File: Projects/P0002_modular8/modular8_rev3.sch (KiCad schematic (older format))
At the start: 14 parts

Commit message: started P0003 LED display, P0002 PCB layout
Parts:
- removed Y?: 16MHz, symbol Crystal_Small
- added C3: 0.1uF, Capacitors_SMD:C_0805, symbol C
- added D1: POW, LEDs:LED-0805, symbol LED
- added D2: SCK, LEDs:LED-0805, symbol LED
- added R1, R2: 680, Resistors_SMD:R_0805, symbol R
- added R3: 10k, Resistors_SMD:R_0805, symbol R
- added R4, R5: 39, Resistors_SMD:R_0805, symbol R
- added U1: LM4040D20IDBZR, Housings_SOT-23_SOT-143_TSOT-6:SOT-23, symbol LM4040D20IDBZR
- added XTAL?1: ABM8-16.000MHZ-10-1-U-T, Libraries - KiCAD:CSMD-ABM8, symbol ABM8-16.000MHZ-10-1-U-T
- C1, C2, C4, C5, C6: renamed from C?; footprint (none) -> Capacitors_SMD:C_0805
- GC1: renamed from GC; footprint (none) -> Resistors_SMD:R_0805
- IC1: renamed from IC?; footprint MLF/QFN32 -> Housings_QFP:TQFP-32_7x7mm_Pitch0.8mm
- J1, J2, J3, J4: renamed from J?; footprint (none) -> Libraries - KiCAD:modular8_rev3_edge
- L1: renamed from L?; footprint (none) -> Resistors_SMD:R_0805
- LDO1: renamed from LDO?; footprint (none) -> Housings_SOT-23_SOT-143_TSOT-6:SOT-23
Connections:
- net RXMCU is gone; now on net RX: IC1.30 ((PCINT16/RXD)PD0)
- net RXOUT is gone; now on net RX: J1.4 (RX/THRU)
- net TXMCU is gone; now on net TX: IC1.31 ((PCINT17/TXD)PD1)
- net TXOUT is gone; now on net TX: J1.6 (TX)
- net 2.048V: now also C3.1, R3.2, U1.1 (2.048V)
- net GND: now also C5.2, C6.2, R1.2, R2.2, XTAL?1.2 (GND), XTAL?1.4 (GND)
- net GNDA: now also C3.2, U1.2 (GND)
- net MISO: now also J1.11 (MISO), J2.1 (MISO)
- net MOSI: now also J1.10 (MOSI), R5.1
- net SCK: now also J1.9 (SCK), D2.2 (A), R4.2
- net at C4.1, IC1.18 (AVCC), L1.2: now also R3.1
- net 3V3: now reaches C2.1, IC1.4 (VCC), IC1.6 (VCC), L1.1, LDO1.2 (OUT)
- net 3V3: now also D1.2 (A)
- net at IC1.7 ((PCINT6/XTAL1/TOSC1)PB6): now also C5.1, XTAL?1.1; no longer C5.2
- net at IC1.8 ((PCINT7/XTAL2/TOSC2)PB7): now also C6.1, XTAL?1.3; no longer C6.2
- net at J2.3 (SCK): now also R4.1; no longer J1.9 (SCK)
- net at J2.4 (MOSI): now also R5.2; no longer J1.10 (MOSI)
- net RXIN renamed RX
- net TXIN renamed TX
- new net: D1.1 (K), R1.1
- new net: D2.1 (K), R2.1
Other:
- note removed: "NEXT STEPS\n--------------\nAdd analog voltage reference\nSort out TX/RX terminators and connections\nAdd indicator LEDs\nProtection of some kind?\n39ohm R on programming pins?"
- moved on the sheet: C1, C2, C5, C6, J3, J4, L1, LDO1

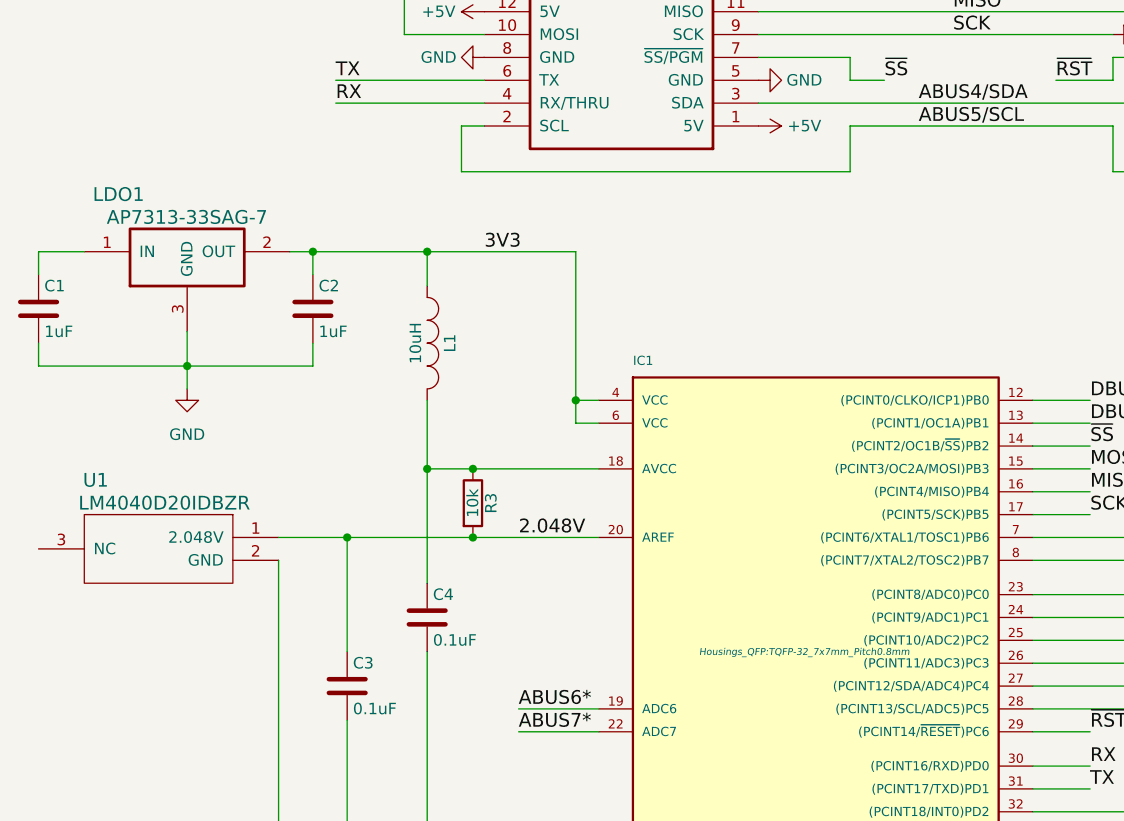
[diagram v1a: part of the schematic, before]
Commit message: started routing modular8_rev3
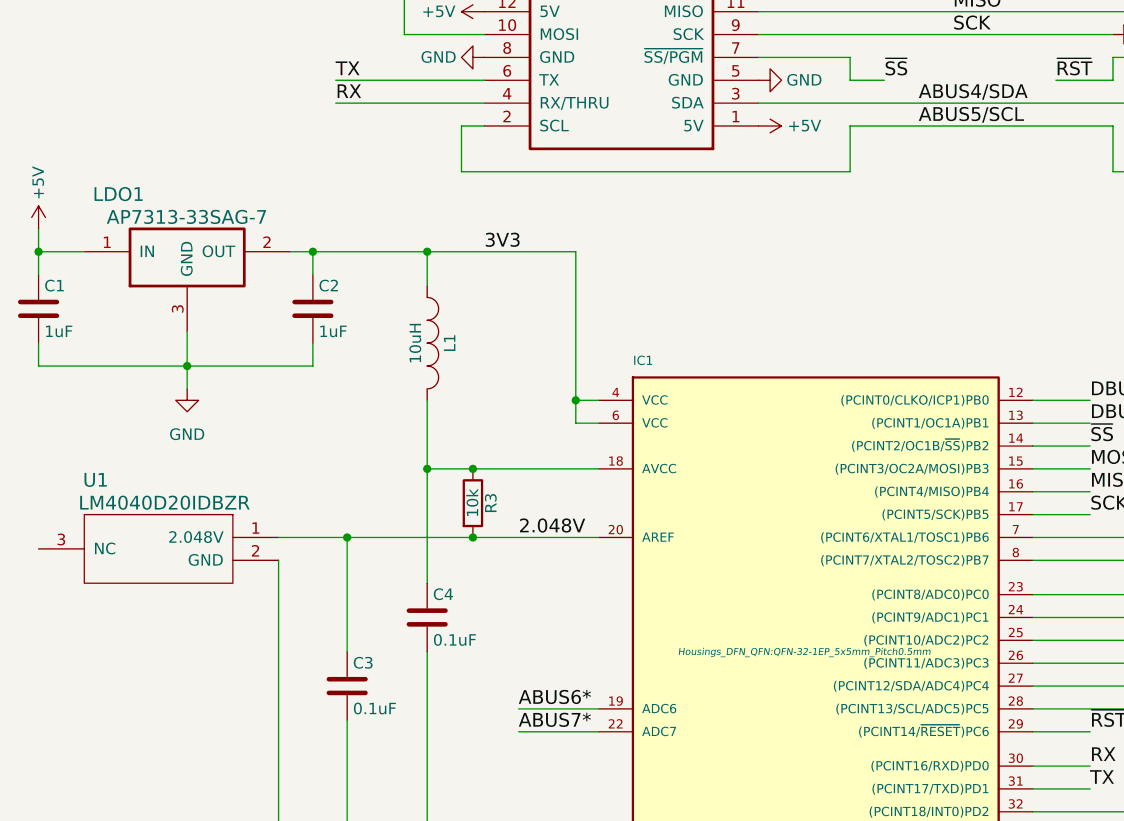
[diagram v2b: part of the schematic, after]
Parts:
- C1, C2, C3, C4, C5, C6: footprint Capacitors_SMD:C_0805 -> Capacitors_SMD:C_0603
- GC1, L1, R1, R2, R3, R4, R5: footprint Resistors_SMD:R_0805 -> Resistors_SMD:R_0603
- IC1: footprint Housings_QFP:TQFP-32_7x7mm_Pitch0.8mm -> Housings_DFN_QFN:QFN-32-1EP_5x5mm_Pitch0.5mm
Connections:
- net +5V: now also C1.1, LDO1.1 (IN)
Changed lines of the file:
@@
 F 0 "IC1" H 4250 5350 40  0000 L BNN
 F 1 "ATMEGA328P-M" H 5400 2700 40  0000 L BNN
-F 2 "Housings_QFP:TQFP-32_7x7mm_Pitch0.8mm" H 5000 4100 30  0000 C CIN
+F 2 "Housings_DFN_QFN:QFN-32-1EP_5x5mm_Pitch0.5mm" H 5000 4100 30  0000 C CIN
 F 3 "" H 5000 4100 60  0000 C CNN
 	1    5000 4100
@@
 F 0 "GC1" V 3830 5300 50  0000 C CNN
 F 1 "0" V 3750 5300 50  0000 C CNN
-F 2 "Resistors_SMD:R_0805" V 3680 5300 30  0001 C CNN
+F 2 "Resistors_SMD:R_0603" V 3680 5300 30  0001 C CNN
 F 3 "" H 3750 5300 30  0000 C CNN
 	1    3750 5300
@@
 F 0 "C5" H 7025 3400 50  0000 L CNN
 F 1 "15pF" H 7025 3200 50  0000 L CNN
-F 2 "Capacitors_SMD:C_0805" H 7038 3150 30  0001 C CNN
+F 2 "Capacitors_SMD:C_0603" H 7038 3150 30  0001 C CNN
 F 3 "" H 7000 3300 60  0000 C CNN
 	1    7000 3300
@@
 F 0 "C6" H 7825 3400 50  0000 L CNN
 F 1 "15pF" H 7825 3200 50  0000 L CNN
-F 2 "Capacitors_SMD:C_0805" H 7838 3150 30  0001 C CNN
+F 2 "Capacitors_SMD:C_0603" H 7838 3150 30  0001 C CNN
 F 3 "" H 7800 3300 60  0000 C CNN
 	1    7800 3300
@@
 F 0 "C2" H 2875 2700 50  0000 L CNN
 F 1 "1uF" H 2875 2500 50  0000 L CNN
-F 2 "Capacitors_SMD:C_0805" H 2888 2450 30  0001 C CNN
+F 2 "Capacitors_SMD:C_0603" H 2888 2450 30  0001 C CNN
 F 3 "" H 2850 2600 60  0000 C CNN
 	1    2850 2600
@@
 F 0 "C1" H 1675 2700 50  0000 L CNN
 F 1 "1uF" H 1675 2500 50  0000 L CNN
-F 2 "Capacitors_SMD:C_0805" H 1688 2450 30  0001 C CNN
+F 2 "Capacitors_SMD:C_0603" H 1688 2450 30  0001 C CNN
 F 3 "" H 1650 2600 60  0000 C CNN
 	1    1650 2600
@@
 F 0 "L1" H 3350 2850 50  0000 C CNN
 F 1 "10uH" H 3350 2700 50  0000 C CNN
-F 2 "Resistors_SMD:R_0805" H 3350 2750 60  0001 C CNN
+F 2 "Resistors_SMD:R_0603" H 3350 2750 60  0001 C CNN
 F 3 "" H 3350 2750 60  0000 C CNN
 	1    3350 2750
@@
 F 0 "C4" H 3375 4050 50  0000 L CNN
 F 1 "0.1uF" H 3375 3850 50  0000 L CNN
-F 2 "Capacitors_SMD:C_0805" H 3388 3800 30  0001 C CNN
+F 2 "Capacitors_SMD:C_0603" H 3388 3800 30  0001 C CNN
 F 3 "" H 3350 3950 60  0000 C CNN
 	1    3350 3950
@@
 F 0 "R3" V 3630 3450 50  0000 C CNN
 F 1 "10k" V 3550 3450 50  0000 C CNN
-F 2 "Resistors_SMD:R_0805" V 3480 3450 30  0001 C CNN
+F 2 "Resistors_SMD:R_0603" V 3480 3450 30  0001 C CNN
 F 3 "" H 3550 3450 30  0000 C CNN
 	1    3550 3450
@@
 F 0 "R1" V 1930 6350 50  0000 C CNN
 F 1 "680" V 1850 6350 50  0000 C CNN
-F 2 "Resistors_SMD:R_0805" V 1780 6350 30  0001 C CNN
+F 2 "Resistors_SMD:R_0603" V 1780 6350 30  0001 C CNN
 F 3 "" H 1850 6350 30  0000 C CNN
 	1    1850 6350
@@
 F 0 "R2" V 2230 6350 50  0000 C CNN
 F 1 "680" V 2150 6350 50  0000 C CNN
-F 2 "Resistors_SMD:R_0805" V 2080 6350 30  0001 C CNN
+F 2 "Resistors_SMD:R_0603" V 2080 6350 30  0001 C CNN
 F 3 "" H 2150 6350 30  0000 C CNN
 	1    2150 6350
@@
 F 0 "R5" V 8480 1150 50  0000 C CNN
 F 1 "39" V 8400 1150 50  0000 C CNN
-F 2 "Resistors_SMD:R_0805" V 8330 1150 30  0001 C CNN
+F 2 "Resistors_SMD:R_0603" V 8330 1150 30  0001 C CNN
 F 3 "" H 8400 1150 30  0000 C CNN
 	1    8400 1150
@@
 F 0 "R4" V 6580 1400 50  0000 C CNN
 F 1 "39" V 6500 1400 50  0000 C CNN
-F 2 "Resistors_SMD:R_0805" V 6430 1400 30  0001 C CNN
+F 2 "Resistors_SMD:R_0603" V 6430 1400 30  0001 C CNN
 F 3 "" H 6500 1400 30  0000 C CNN
 	1    6500 1400
@@
 F 0 "C3" H 3025 4350 50  0000 L CNN
 F 1 "0.1uF" H 3025 4150 50  0000 L CNN
-F 2 "Capacitors_SMD:C_0805" H 3038 4100 30  0001 C CNN
+F 2 "Capacitors_SMD:C_0603" H 3038 4100 30  0001 C CNN
 F 3 "" H 3000 4250 60  0000 C CNN
 	1    3000 4250
@@
 	1850 2350 1650 2350
 Wire Wire Line
-	1650 2350 1650 2450
+	1650 2250 1650 2450
 Wire Wire Line
 	2850 2450 2850 2350
@@
 	7800 3150 8050 3150
 Connection ~ 8050 3150
+$Comp
+L +5V #PWR?
+U 1 1 56249081
+P 1650 2250
+F 0 "#PWR?" H 1650 2100 50  0001 C CNN
+F 1 "+5V" V 1650 2450 50  0000 C CNN
+F 2 "" H 1650 2250 60  0000 C CNN
+F 3 "" H 1650 2250 60  0000 C CNN
+	1    1650 2250
+	1    0    0    -1
+$EndComp
+Connection ~ 1650 2350
 $EndSCHEMATC

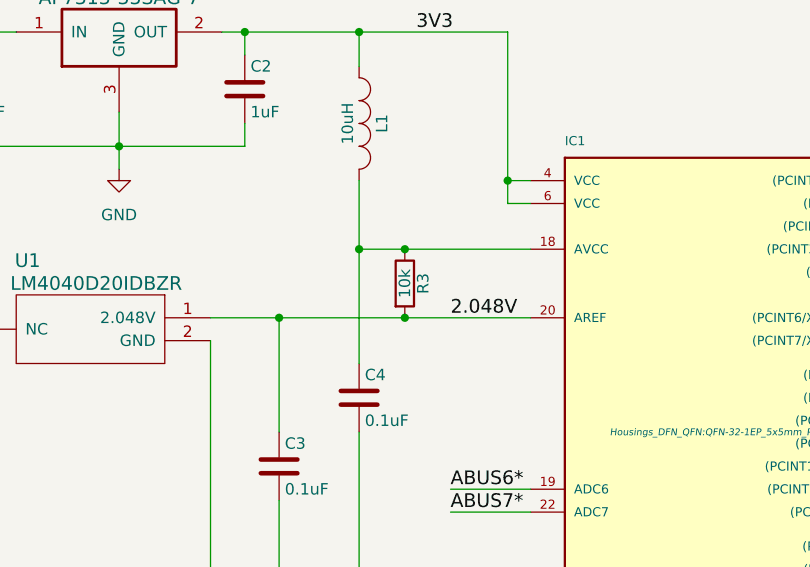
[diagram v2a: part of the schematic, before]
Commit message: changed 10k to 1k for vref m8_rev3
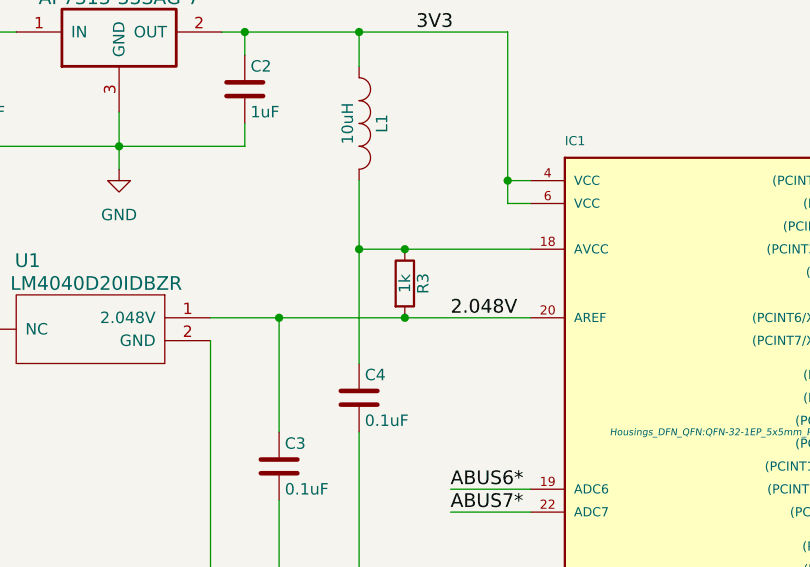
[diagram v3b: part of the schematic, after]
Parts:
- R3: value 10k -> 1k
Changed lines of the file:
@@
 P 3550 3450
 F 0 "R3" V 3630 3450 50  0000 C CNN
-F 1 "10k" V 3550 3450 50  0000 C CNN
+F 1 "1k" V 3550 3450 50  0000 C CNN
 F 2 "Resistors_SMD:R_0603" V 3480 3450 30  0001 C CNN
 F 3 "" H 3550 3450 30  0000 C CNN
@@
 Connection ~ 8050 3150
 $Comp
-L +5V #PWR?
+L +5V #PWR022
 U 1 1 56249081
 P 1650 2250
-F 0 "#PWR?" H 1650 2100 50  0001 C CNN
+F 0 "#PWR022" H 1650 2100 50  0001 C CNN
 F 1 "+5V" V 1650 2450 50  0000 C CNN
 F 2 "" H 1650 2250 60  0000 C CNN
